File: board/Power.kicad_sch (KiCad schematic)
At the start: 12 parts, among them J3 5-1775444-8, U9 TPS61230DRC

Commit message: worked on new version with rp2350
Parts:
- removed C13, C2: 22u, Capacitor_SMD:C_0402_1005Metric, symbol Device:C_Small
- removed R10: 100k, Resistor_SMD:R_0603_1608Metric, symbol Device:R_Small_US
- removed R9: 402k, Resistor_SMD:R_0603_1608Metric, symbol Device:R_Small_US
- added C14: 10u, Capacitor_SMD:C_0402_1005Metric, symbol Device:C_Small
- C1: value 22u -> 10u
- C12: value 10n -> 8.2n
- C3: value 22u -> 4.7u
- C9: value 18p -> 10u; MFR# (none) -> GRM158R61A226ME15D
- L1: value 1uH -> 18.1uH
- R11: value 1M -> 100K
- U9: value TPS61230DRC -> TPS61232DRC
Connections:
- net +5V: now also U9.7 (FB); no longer C9.1
- net GND: now also C9.2, C14.2
- net power in: no longer C1.1, J3.1, J3.2, J3.3, J3.4, L1.1, U9.10 (VIN), U9.9 (EN)
- new net: C1.1, C14.1, C9.1, J3.1, J3.2, J3.3, J3.4, L1.1, U9.10 (VIN), U9.9 (EN)

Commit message: almost v0.3
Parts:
- L1: value 18.1uH -> 1uH; footprint Inductor_SMD:L_Coilcraft_XxL4020 -> MDA4020:MDA4020
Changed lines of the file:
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@@
 			)
 		)
-		(property "Value" "18.1uH"
+		(property "Value" "1uH"
 			(at 153.67 85.09 90)
 			(effects
@@
 			)
 		)
-		(property "Footprint" "Inductor_SMD:L_Coilcraft_XxL4020"
+		(property "Footprint" "MDA4020:MDA4020"
 			(at 153.67 86.36 0)
 			(effects
@@
 			)
 		)
-		(property "Description" ""
+		(property "Description" "L_Coilcraft_XxL4020"
 			(at 153.67 86.36 0)
 			(effects

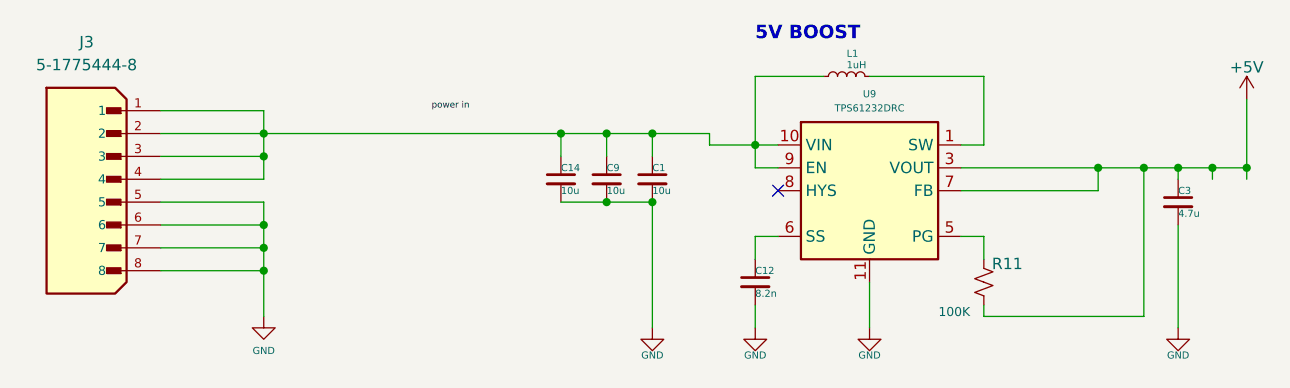
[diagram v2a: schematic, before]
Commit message: going to add the magnetic transformer which will messs a lot of stuff up
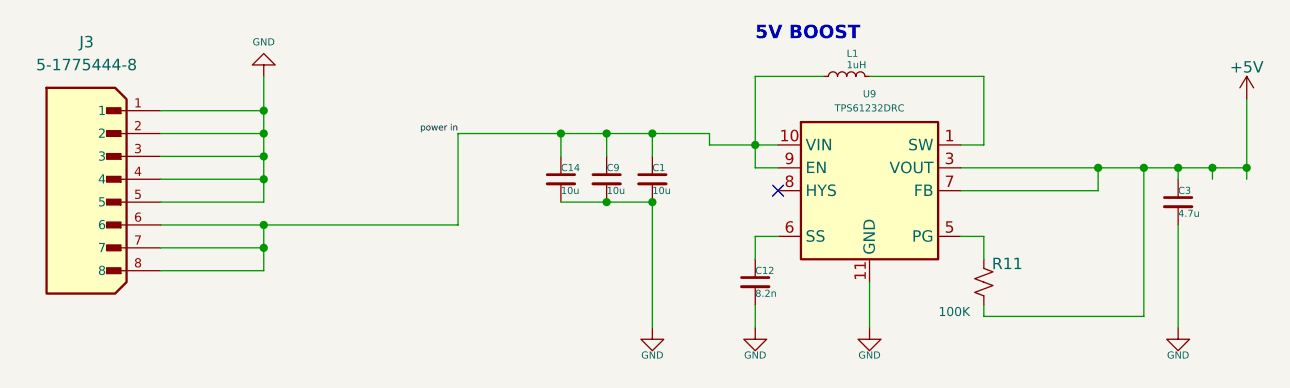
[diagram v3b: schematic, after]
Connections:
- net GND: now also J3.1, J3.2, J3.3, J3.4; no longer J3.6, J3.7, J3.8
- net power in: now also C1.1, C14.1, C9.1, J3.6, J3.7, J3.8, L1.1, U9.10 (VIN), U9.9 (EN)

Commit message: should be the last build
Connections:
- net GND: now also J3.6, J3.7, J3.8; no longer J3.1, J3.2, J3.3
- net power in: now also J3.1, J3.2, J3.3; no longer J3.6, J3.7, J3.8
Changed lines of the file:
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@@
 	)
 	(junction
-		(at 88.9 95.25)
+		(at 88.9 107.95)
 		(diameter 0)
 		(color 0 0 0 0)
@@
 	)
 	(junction
+		(at 88.9 100.33)
+		(diameter 0)
+		(color 0 0 0 0)
+	)
+	(junction
 		(at 132.08 100.33)
 		(diameter 0)
@@
 	)
 	(junction
-		(at 88.9 90.17)
-		(diameter 0)
-		(color 0 0 0 0)
-	)
-	(junction
 		(at 127 100.33)
 		(diameter 0)
 		(color 0 0 0 0)
 	)
-	(junction
-		(at 88.9 97.79)
-		(diameter 0)
-		(color 0 0 0 0)
-	)
 	(no_connect
 		(at 146.05 99.06)
@@
 	(wire
 		(pts
+			(xy 88.9 92.71) (xy 121.92 92.71)
+		)
+		(stroke
+			(width 0)
+			(type default)
+		)
+	)
+	(wire
+		(pts
 			(xy 127 92.71) (xy 127 95.25)
 		)
@@
 	(wire
 		(pts
-			(xy 110.49 102.87) (xy 110.49 92.71)
-		)
-		(stroke
-			(width 0)
-			(type default)
-		)
-	)
-	(wire
-		(pts
 			(xy 166.37 96.52) (xy 181.61 96.52)
 		)
@@
 	(wire
 		(pts
+			(xy 88.9 97.79) (xy 88.9 100.33)
+		)
+		(stroke
+			(width 0)
+			(type default)
+		)
+	)
+	(wire
+		(pts
 			(xy 77.47 102.87) (xy 88.9 102.87)
 		)
@@
 	(wire
 		(pts
+			(xy 88.9 100.33) (xy 88.9 102.87)
+		)
+		(stroke
+			(width 0)
+			(type default)
+		)
+	)
+	(wire
+		(pts
 			(xy 143.51 93.98) (xy 143.51 86.36)
 		)
@@
 	(wire
 		(pts
-			(xy 110.49 92.71) (xy 121.92 92.71)
-		)
-		(stroke
-			(width 0)
-			(type default)
-		)
-	)
-	(wire
-		(pts
 			(xy 156.21 86.36) (xy 168.91 86.36)
 		)
@@
 	(wire
 		(pts
-			(xy 88.9 86.36) (xy 88.9 90.17)
-		)
-		(stroke
-			(width 0)
-			(type default)
-		)
-	)
-	(wire
-		(pts
 			(xy 168.91 93.98) (xy 166.37 93.98)
 		)
@@
 	(wire
 		(pts
-			(xy 88.9 97.79) (xy 88.9 95.25)
-		)
-		(stroke
-			(width 0)
-			(type default)
-		)
-	)
-	(wire
-		(pts
 			(xy 77.47 105.41) (xy 88.9 105.41)
 		)
@@
 	(wire
 		(pts
+			(xy 88.9 107.95) (xy 88.9 114.3)
+		)
+		(stroke
+			(width 0)
+			(type default)
+		)
+	)
+	(wire
+		(pts
 			(xy 143.51 104.14) (xy 143.51 106.68)
 		)
@@
 	(wire
 		(pts
-			(xy 88.9 100.33) (xy 88.9 97.79)
-		)
-		(stroke
-			(width 0)
-			(type default)
-		)
-	)
-	(wire
-		(pts
 			(xy 138.43 93.98) (xy 143.51 93.98)
-		)
-		(stroke
-			(width 0)
-			(type default)
-		)
-	)
-	(wire
-		(pts
-			(xy 88.9 102.87) (xy 110.49 102.87)
 		)
 		(stroke
@@
 	(symbol
 		(lib_id "WIreless_Receiver_with_QI_Charging-rescue:GND-power")
-		(at 88.9 86.36 180)
+		(at 88.9 114.3 0)
 		(unit 1)
 		(exclude_from_sim no)
@@
 		(dnp no)
 		(property "Reference" "#PWR017"
-			(at 88.9 80.01 0)
+			(at 88.9 120.65 0)
 			(effects
 				(font
@@
 		)
 		(property "Value" "GND"
-			(at 88.9 82.55 0)
+			(at 88.9 118.11 0)
 			(effects
 				(font
@@
 		)
 		(property "Footprint" ""
-			(at 88.9 86.36 0)
+			(at 88.9 114.3 0)
 			(effects
 				(font
@@
 		)
 		(property "Datasheet" ""
-			(at 88.9 86.36 0)
+			(at 88.9 114.3 0)
 			(effects
 				(font
@@
 		)
 		(property "Description" ""
-			(at 88.9 86.36 0)
-			(effects
-				(font
+			(at 88.9 114.3 0)
+			(effects
+				(font
